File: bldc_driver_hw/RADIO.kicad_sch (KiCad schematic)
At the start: 18 parts, among them SW2 SW_Push, SW3 SW_Push, U8 ESP32-C6-MINI-1

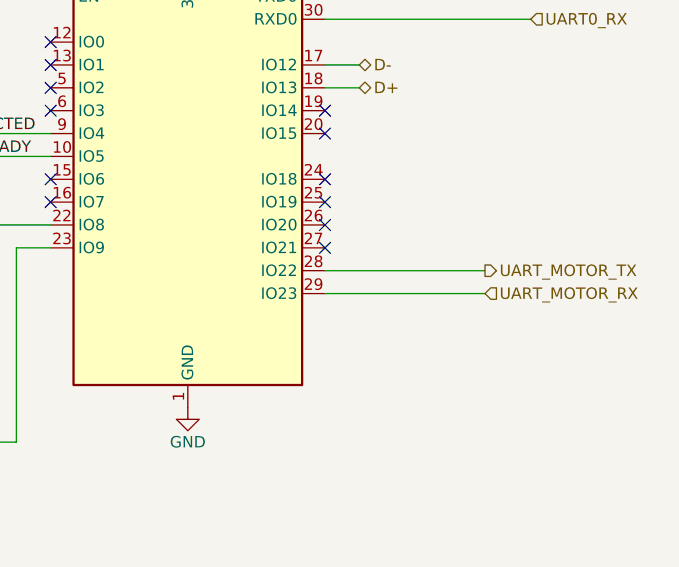
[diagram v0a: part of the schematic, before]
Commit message: changed hrtim to tim1
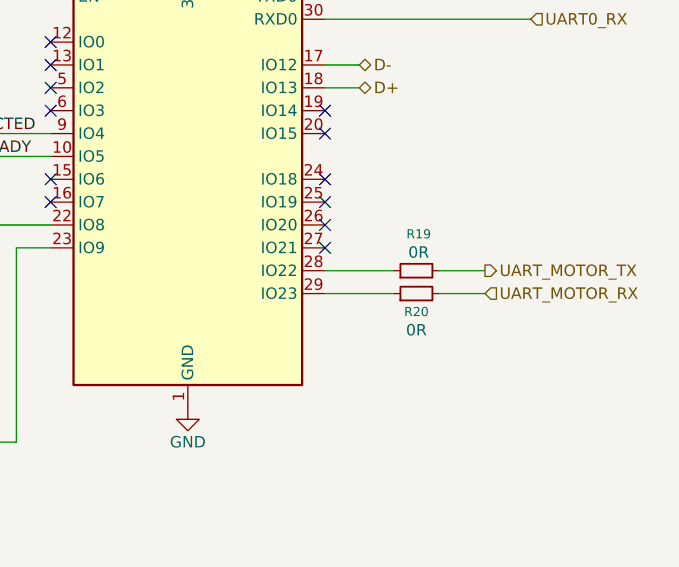
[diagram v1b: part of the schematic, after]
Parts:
- added R19, R20: 0R, Resistor_SMD:R_0402_1005Metric, symbol Device:R_Small
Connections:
- net UART_MOTOR_RX: now also R20.2; no longer U8.29 (IO23)
- net UART_MOTOR_TX: now also R19.2; no longer U8.28 (IO22)
- new net: R20.1, U8.29 (IO23)
- new net: R19.1, U8.28 (IO22)
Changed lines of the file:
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@@
+	(wire
+		(pts
+			(xy 137.16 102.87) (xy 142.24 102.87)
+		)
+		(stroke
+			(width 0)
+			(type default)
+		)
+	)
 	(wire
 		(pts
@@
 	(wire
 		(pts
-			(xy 124.46 102.87) (xy 142.24 102.87)
+			(xy 137.16 100.33) (xy 142.24 100.33)
+		)
+		(stroke
+			(width 0)
+			(type default)
+		)
+	)
+	(wire
+		(pts
+			(xy 124.46 102.87) (xy 132.08 102.87)
 		)
 		(stroke
@@
 	(wire
 		(pts
-			(xy 124.46 100.33) (xy 142.24 100.33)
+			(xy 124.46 100.33) (xy 132.08 100.33)
 		)
 		(stroke
@@
 				(path "/7f946e06-72d3-4343-93fe-84e8bb5001be/b1c55804-10de-45a9-b77e-813878bb2e3e"
 					(reference "R28")
+					(unit 1)
+				)
+			)
+		)
+	)
+	(symbol
+		(lib_id "Device:R_Small")
+		(at 134.62 102.87 90)
+		(unit 1)
+		(exclude_from_sim no)
+		(in_bom yes)
+		(on_board yes)
+		(dnp no)
+		(property "Reference" "R20"
+			(at 134.62 104.902 90)
+			(effects
+				(font
+					(size 1.016 1.016)
+				)
+			)
+		)
+		(property "Value" "0R"
+			(at 134.62 106.934 90)
+			(effects
+				(font
+					(size 1.27 1.27)
+				)
+			)
+		)
+		(property "Footprint" "Resistor_SMD:R_0402_1005Metric"
+			(at 134.62 102.87 0)
+			(effects
+				(font
+					(size 1.27 1.27)
+				)
+				(hide yes)
+			)
+		)
+		(property "Datasheet" "~"
+			(at 134.62 102.87 0)
+			(effects
+				(font
+					(size 1.27 1.27)
+				)
+				(hide yes)
+			)
+		)
+		(property "Description" "Resistor, small symbol"
+			(at 134.62 102.87 0)
+			(effects
+				(font
+					(size 1.27 1.27)
+				)
+				(hide yes)
+			)
+		)
+		(property "LCSC" "C17168"
+			(at 134.62 102.87 0)
+			(effects
+				(font
+					(size 1.27 1.27)
+				)
+				(hide yes)
+			)
+		)
+		(pin "2"
+		)
+		(pin "1"
+		)
+		(instances
+			(project "bldc_driver_hw"
+				(path "/7f946e06-72d3-4343-93fe-84e8bb5001be/b1c55804-10de-45a9-b77e-813878bb2e3e"
+					(reference "R20")
 					(unit 1)
 				)
@@
 					(unit 1)
 				)
+			)
+		)
+	)
+	(symbol
+		(lib_id "Device:R_Small")
+		(at 134.62 100.33 90)
+		(unit 1)
+		(exclude_from_sim no)
+		(in_bom yes)
+		(on_board yes)
+		(dnp no)
+		(property "Reference" "R19"
+			(at 134.874 96.266 90)
+			(effects
+				(font
+					(size 1.016 1.016)
+				)
+			)
+		)
+		(property "Value" "0R"
+			(at 134.874 98.298 90)
+			(effects
+				(font
+					(size 1.27 1.27)
+				)
+			)
+		)
+		(property "Footprint" "Resistor_SMD:R_0402_1005Metric"
+			(at 134.62 100.33 0)
+			(effects
+				(font
+					(size 1.27 1.27)
+				)
+				(hide yes)
+			)
+		)
+		(property "Datasheet" "~"
+			(at 134.62 100.33 0)
+			(effects
+				(font
+					(size 1.27 1.27)
+				)
+				(hide yes)
+			)
+		)
+		(property "Description" "Resistor, small symbol"
+			(at 134.62 100.33 0)
+			(effects
+				(font
+					(size 1.27 1.27)
+				)
+				(hide yes)
+			)
+		)
+		(property "LCSC" "C17168"
+			(at 134.62 100.33 0)
+			(effects
+				(font
+					(size 1.27 1.27)
+				)
+				(hide yes)
+			)
+		)
+		(pin "2"
+		)
+		(pin "1"
+		)
+		(instances
+			(project "bldc_driver_hw"
+				(path "/7f946e06-72d3-4343-93fe-84e8bb5001be/b1c55804-10de-45a9-b77e-813878bb2e3e"
+					(reference "R19")
+					(unit 1)
+				)
